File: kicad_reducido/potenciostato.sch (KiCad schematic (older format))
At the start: 11 parts, among them J1 Conn_01x03_Female, J3 Conn_01x03_Male, U1 OP77, U2 TL082, U3 OP77, U4 OP77

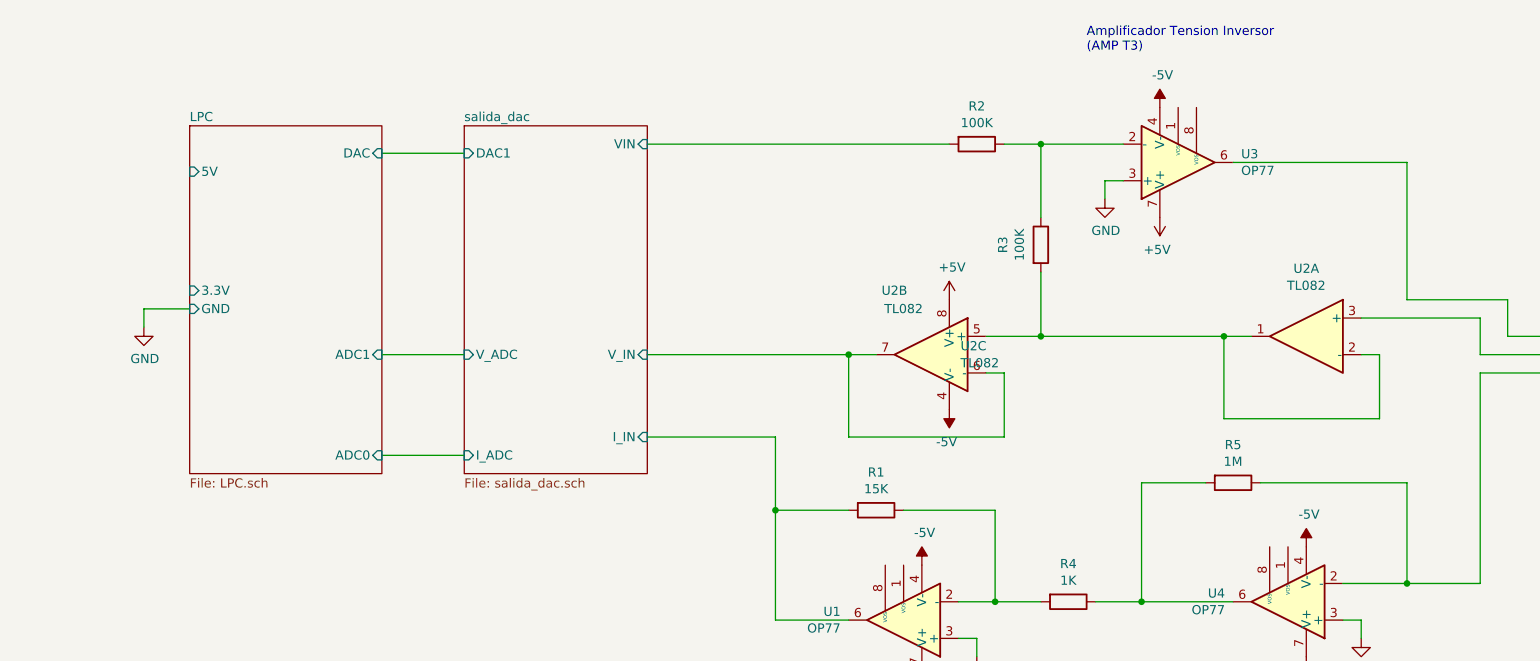
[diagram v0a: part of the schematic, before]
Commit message: ruteado kicad reducido parcialmente completo
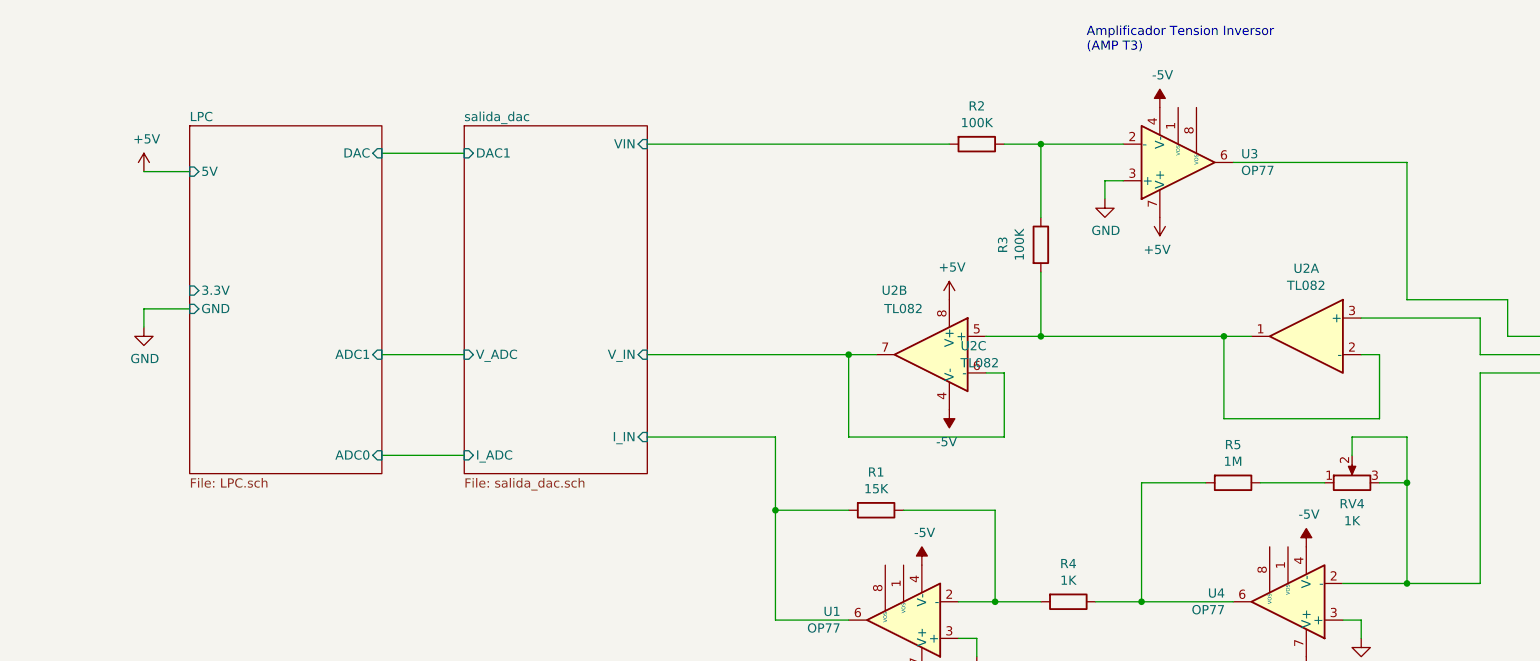
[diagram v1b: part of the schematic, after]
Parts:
- added RV4: 1K, Potentiometer_THT:Potentiometer_Bourns_3266Y_Vertical, symbol salida_dac-rescue:R_POT-Device
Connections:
- net at J3.1 (Pin_1), U4.2 (-): now also RV4.2, RV4.3; no longer R5.1
- new net: R5.1, RV4.1
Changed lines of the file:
@@
 	7950 3250 8100 3250
-Wire Wire Line
-	8950 4050 8950 4600
 Wire Wire Line
 	8950 4600 8600 4600
@@
 	-1   0    0    1
 $EndComp
-Wire Wire Line
-	8150 4050 8950 4050
 NoConn ~ 5700 7300
 $Comp
@@
 F7 "V_ADC" I L 3800 3350 50
 $EndSheet
+$Comp
+L potenciostato-rescue:+5V-power #PWR0109
+U 1 1 617B6A7C
+P 2050 2350
+F 0 "#PWR0109" H 2050 2200 50  0001 C CNN
+F 1 "+5V" H 2065 2527 50  0000 C CNN
+F 2 "" H 2050 2350 50  0001 C CNN
+F 3 "" H 2050 2350 50  0001 C CNN
+	1    2050 2350
+	1    0    0    -1
+$EndComp
+Wire Wire Line
+	2300 2350 2050 2350
+$Comp
+L salida_dac-rescue:R_POT-Device RV?
+U 1 1 617C0F32
+P 8650 4050
+AR Path="/6013BA2D/617C0F32" Ref="RV?"  Part="1"
+AR Path="/617C0F32" Ref="RV4"  Part="1"
+F 0 "RV4" V 8534 4050 50  0000 C CNN
+F 1 "1K" V 8441 4050 50  0000 C CNN
+F 2 "Potentiometer_THT:Potentiometer_Bourns_3266Y_Vertical" H 8650 4050 50  0001 C CNN
+F 3 "~" H 8650 4050 50  0001 C CNN
+	1    8650 4050
+	0    -1   -1   0
+$EndComp
+Wire Wire Line
+	8150 4050 8500 4050
+Wire Wire Line
+	8800 4050 8950 4050
+Wire Wire Line
+	8650 3800 8950 3800
+Connection ~ 8950 4050
+Wire Wire Line
+	8950 4050 8950 4600
+Wire Wire Line
+	8950 3800 8950 4050
+Wire Wire Line
+	8650 3800 8650 3900
 $EndSCHEMATC

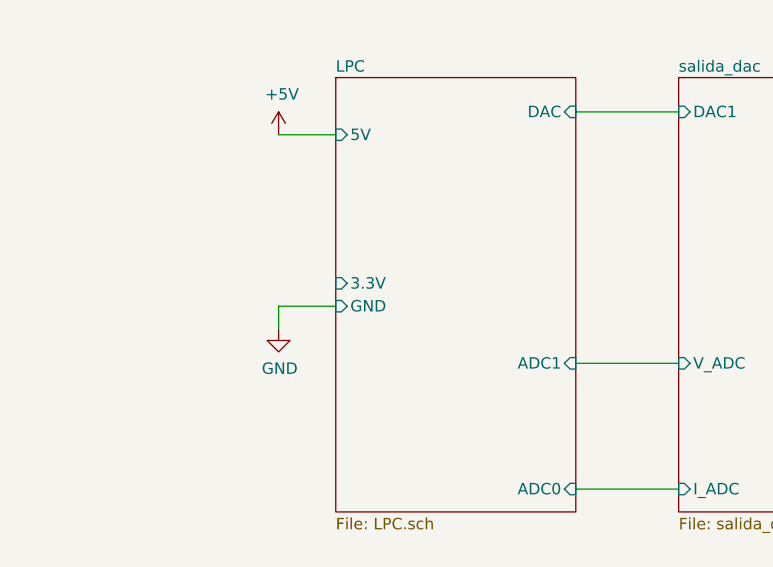
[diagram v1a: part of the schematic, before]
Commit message: pcb reducido en 10x10
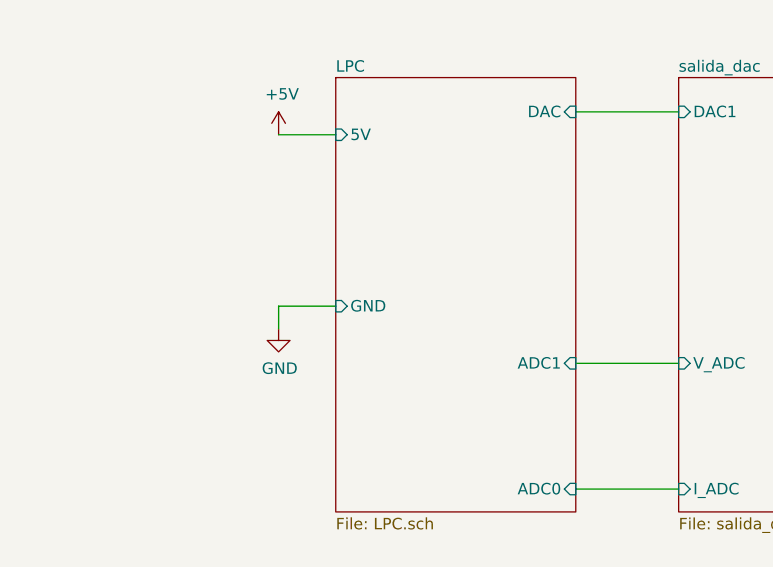
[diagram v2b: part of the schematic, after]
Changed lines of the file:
@@
 F1 "LPC.sch" 50
 F2 "GND" I L 2300 3100 50
-F3 "3.3V" I L 2300 3000 50
-F4 "DAC" I R 3350 2250 50
-F5 "ADC1" I R 3350 3350 50
-F6 "ADC0" I R 3350 3900 50
-F7 "5V" I L 2300 2350 50
+F3 "DAC" I R 3350 2250 50
+F4 "ADC1" I R 3350 3350 50
+F5 "ADC0" I R 3350 3900 50
+F6 "5V" I L 2300 2350 50
 $EndSheet
 $Sheet

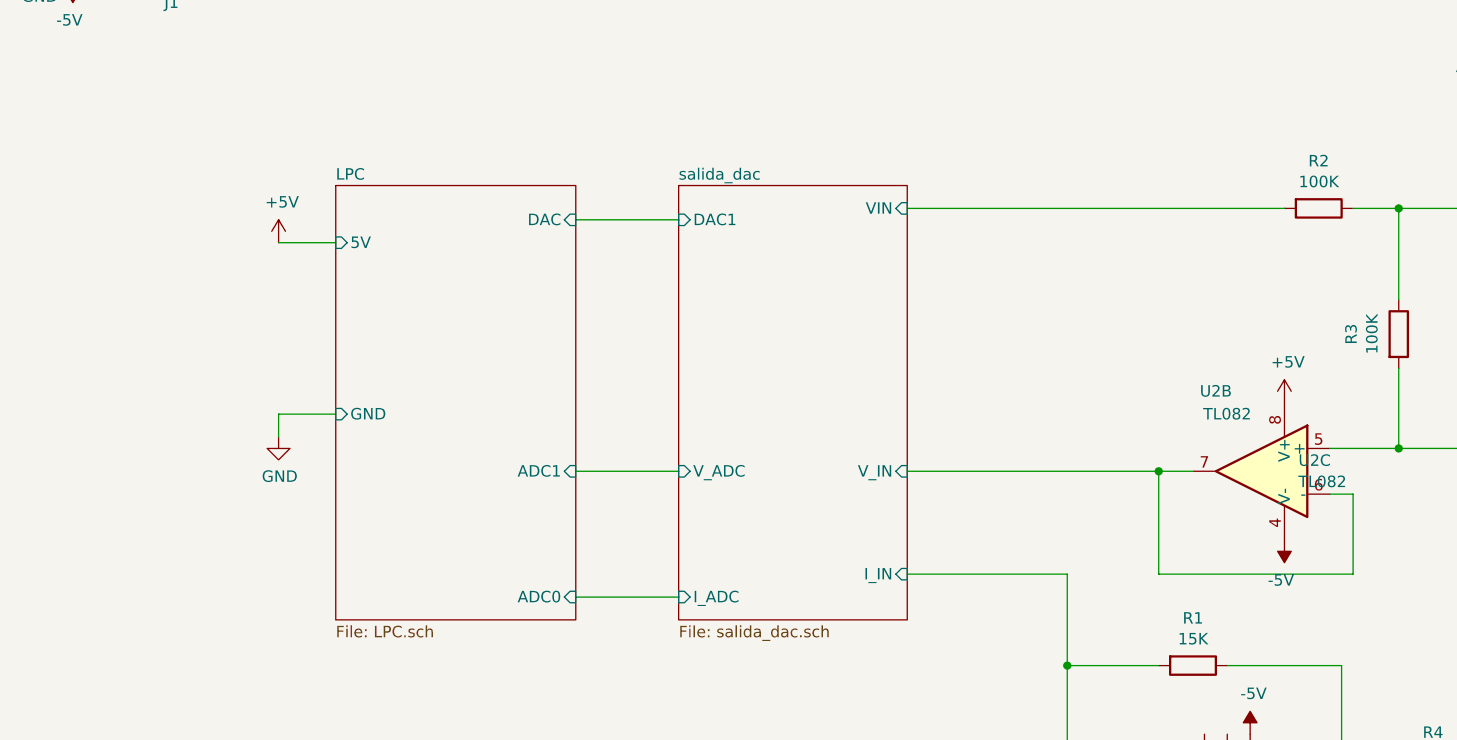
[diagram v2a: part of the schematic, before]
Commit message: pcb reducido listo falta revisar
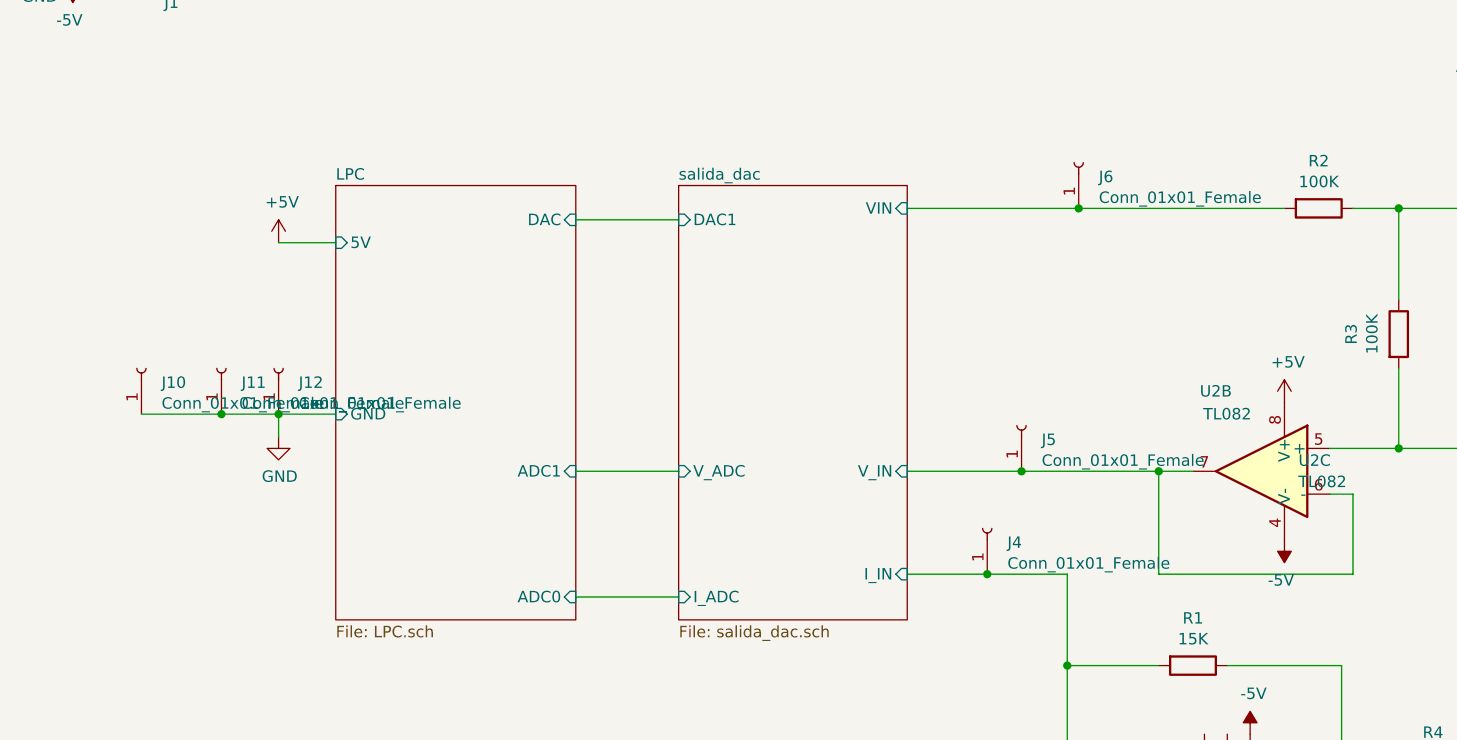
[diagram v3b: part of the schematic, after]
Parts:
- added J10, J11, J12, J4, J5, J6: Conn_01x01_Female, Connector_PinHeader_2.54mm:PinHeader_1x01_P2.54mm_Vertical, symbol Connector:Conn_01x01_Female
- R3: footprint Resistor_THT:R_Axial_DIN0207_L6.3mm_D2.5mm_P7.62mm_Horizontal -> Resistor_THT:R_Axial_DIN0207_L6.3mm_D2.5mm_P10.16mm_Horizontal
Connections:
- net GND: now also J10.1 (Pin_1), J11.1 (Pin_1), J12.1 (Pin_1)
- net salida_dac/I_IN: now also J4.1 (Pin_1)
- net salida_dac/VIN: now also J6.1 (Pin_1)
- net salida_dac/V_IN: now also J5.1 (Pin_1)
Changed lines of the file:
@@
 F 0 "R3" V 6743 2750 50  0000 C CNN
 F 1 "100K" V 6834 2750 50  0000 C CNN
-F 2 "Resistor_THT:R_Axial_DIN0207_L6.3mm_D2.5mm_P7.62mm_Horizontal" V 6880 2750 50  0001 C CNN
+F 2 "Resistor_THT:R_Axial_DIN0207_L6.3mm_D2.5mm_P10.16mm_Horizontal" V 6880 2750 50  0001 C CNN
 F 3 "~" H 6950 2750 50  0001 C CNN
 	1    6950 2750
@@
 Connection ~ 6950 3250
 Wire Wire Line
-	4800 2200 6450 2200
-Wire Wire Line
-	5900 3350 4800 3350
+	4800 2200 5550 2200
+Wire Wire Line
+	5900 3350 5300 3350
 Connection ~ 5900 3350
 Wire Wire Line
-	4800 3800 5500 3800
+	4800 3800 5150 3800
 Wire Wire Line
 	5500 3800 5500 4200
@@
 Wire Wire Line
 	8650 3800 8650 3900
+$Comp
+L Connector:Conn_01x01_Female J4
+U 1 1 6185139C
+P 5150 3600
+F 0 "J4" V 5088 3512 50  0000 R CNN
+F 1 "Conn_01x01_Female" V 4997 3512 50  0000 R CNN
+F 2 "Connector_PinHeader_2.54mm:PinHeader_1x01_P2.54mm_Vertical" H 5150 3600 50  0001 C CNN
+F 3 "~" H 5150 3600 50  0001 C CNN
+	1    5150 3600
+	0    -1   -1   0
+$EndComp
+Connection ~ 5150 3800
+Wire Wire Line
+	5150 3800 5500 3800
+$Comp
+L Connector:Conn_01x01_Female J5
+U 1 1 61851AC8
+P 5300 3150
+F 0 "J5" V 5238 3062 50  0000 R CNN
+F 1 "Conn_01x01_Female" V 5147 3062 50  0000 R CNN
+F 2 "Connector_PinHeader_2.54mm:PinHeader_1x01_P2.54mm_Vertical" H 5300 3150 50  0001 C CNN
+F 3 "~" H 5300 3150 50  0001 C CNN
+	1    5300 3150
+	0    -1   -1   0
+$EndComp
+Connection ~ 5300 3350
+Wire Wire Line
+	5300 3350 4800 3350
+$Comp
+L Connector:Conn_01x01_Female J6
+U 1 1 61851D11
+P 5550 2000
+F 0 "J6" V 5488 1912 50  0000 R CNN
+F 1 "Conn_01x01_Female" V 5397 1912 50  0000 R CNN
+F 2 "Connector_PinHeader_2.54mm:PinHeader_1x01_P2.54mm_Vertical" H 5550 2000 50  0001 C CNN
+F 3 "~" H 5550 2000 50  0001 C CNN
+	1    5550 2000
+	0    -1   -1   0
+$EndComp
+Connection ~ 5550 2200
+Wire Wire Line
+	5550 2200 6450 2200
+$Comp
+L Connector:Conn_01x01_Female J12
+U 1 1 6185D9DF
+P 2050 2900
+F 0 "J12" V 1988 2812 50  0000 R CNN
+F 1 "Conn_01x01_Female" V 1897 2812 50  0000 R CNN
+F 2 "Connector_PinHeader_2.54mm:PinHeader_1x01_P2.54mm_Vertical" H 2050 2900 50  0001 C CNN
+F 3 "~" H 2050 2900 50  0001 C CNN
+	1    2050 2900
+	0    -1   -1   0
+$EndComp
+Connection ~ 2050 3100
+$Comp
+L Connector:Conn_01x01_Female J11
+U 1 1 6185DEE6
+P 1800 2900
+F 0 "J11" V 1738 2812 50  0000 R CNN
+F 1 "Conn_01x01_Female" V 1647 2812 50  0000 R CNN
+F 2 "Connector_PinHeader_2.54mm:PinHeader_1x01_P2.54mm_Vertical" H 1800 2900 50  0001 C CNN
+F 3 "~" H 1800 2900 50  0001 C CNN
+	1    1800 2900
+	0    -1   -1   0
+$EndComp
+$Comp
+L Connector:Conn_01x01_Female J10
+U 1 1 6185E017
+P 1450 2900
+F 0 "J10" V 1388 2812 50  0000 R CNN
+F 1 "Conn_01x01_Female" V 1297 2812 50  0000 R CNN
+F 2 "Connector_PinHeader_2.54mm:PinHeader_1x01_P2.54mm_Vertical" H 1450 2900 50  0001 C CNN
+F 3 "~" H 1450 2900 50  0001 C CNN
+	1    1450 2900
+	0    -1   -1   0
+$EndComp
+Wire Wire Line
+	1800 3100 2050 3100
+Wire Wire Line
+	1450 3100 1800 3100
+Connection ~ 1800 3100
 $EndSCHEMATC

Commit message: modificaciones R
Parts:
- R1: value 15K -> 33K
- R4: value 1K -> 10K
- R5: value 1M -> 0K
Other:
- note added: "Calculamos para una entrada de 1mA \npara que no sature en las primeras mediciones"
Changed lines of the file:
@@
 P 8000 4050
 F 0 "R5" V 7793 4050 50  0000 C CNN
-F 1 "1M" V 7884 4050 50  0000 C CNN
+F 1 "0K" V 7884 4050 50  0000 C CNN
 F 2 "Resistor_THT:R_Axial_DIN0207_L6.3mm_D2.5mm_P7.62mm_Horizontal" V 7930 4050 50  0001 C CNN
 F 3 "~" H 8000 4050 50  0001 C CNN
@@
 P 6050 4200
 F 0 "R1" V 5843 4200 50  0000 C CNN
-F 1 "15K" V 5934 4200 50  0000 C CNN
+F 1 "33K" V 5934 4200 50  0000 C CNN
 F 2 "Resistor_THT:R_Axial_DIN0207_L6.3mm_D2.5mm_P7.62mm_Horizontal" V 5980 4200 50  0001 C CNN
 F 3 "~" H 6050 4200 50  0001 C CNN
@@
 P 7100 4700
 F 0 "R4" V 6893 4700 50  0000 C CNN
-F 1 "1K" V 6984 4700 50  0000 C CNN
+F 1 "10K" V 6984 4700 50  0000 C CNN
 F 2 "Resistor_THT:R_Axial_DIN0207_L6.3mm_D2.5mm_P7.62mm_Horizontal" V 7030 4700 50  0001 C CNN
 F 3 "~" H 7100 4700 50  0001 C CNN
@@
 	1450 3100 1800 3100
 Connection ~ 1800 3100
+Text Notes 9000 4850 0    50   ~ 0
+Calculamos para una entrada de 1mA \npara que no sature en las primeras mediciones
 $EndSCHEMATC
